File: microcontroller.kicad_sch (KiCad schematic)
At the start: 14 parts, among them SW201 SW_Push, U201 ESP32-S3-PICO-1-N8R2

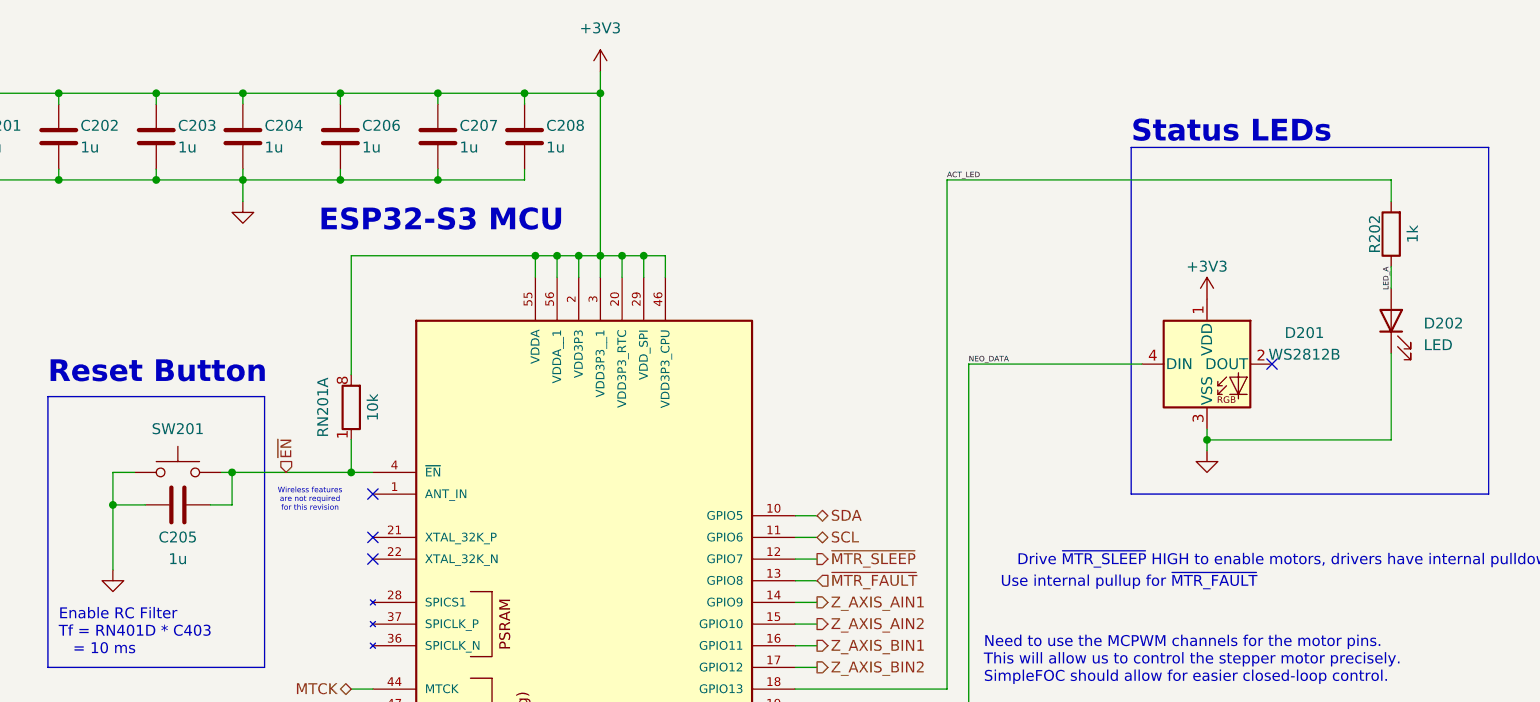
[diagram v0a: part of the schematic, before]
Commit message: Changed motor power supply
Removed 5V power rail. Migrated 3.3V rail to TPS62160
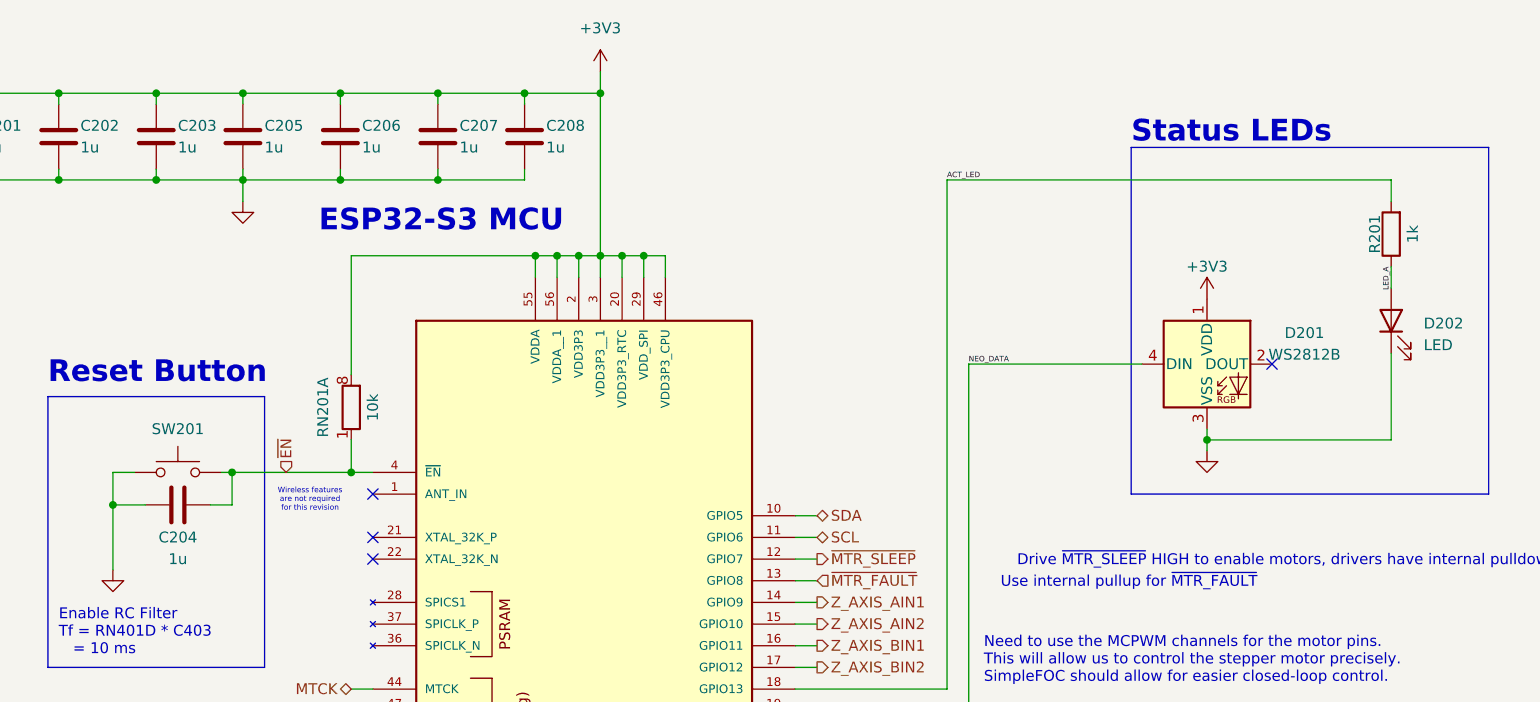
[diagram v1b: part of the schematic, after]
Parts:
- U201: footprint ESP32-S3-PICO-1-N8R2:PQFN40P700X700X106-57N -> SL_ST Tweezers:PQFN40P700X700X106-57N
- renumbered C205 to C204, C204 to C205, R202 to R201
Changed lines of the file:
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@@
 		(on_board yes)
 		(dnp no)
-		(property "Reference" "C204"
+		(property "Reference" "C205"
 			(at 102.87 27.94 0)
 			(effects
@@
 			(project "Vacuum_Tweezers"
 				(path "/25b5e35e-9397-4bb5-a91c-fc11ba49a08d/466683da-b970-4afc-a558-6e1093941948"
-					(reference "C204")
+					(reference "C205")
 					(unit 1)
 				)
@@
 		(on_board yes)
 		(dnp no)
-		(property "Reference" "#PWR0208"
+		(property "Reference" "#PWR0205"
 			(at 213.36 52.07 0)
 			(effects
@@
 			(project "Vacuum_Tweezers"
 				(path "/25b5e35e-9397-4bb5-a91c-fc11ba49a08d/466683da-b970-4afc-a558-6e1093941948"
-					(reference "#PWR0208")
+					(reference "#PWR0205")
 					(unit 1)
 				)
@@
 		(on_board yes)
 		(dnp no)
-		(property "Reference" "#PWR0201"
+		(property "Reference" "#PWR0203"
 			(at 142.24 25.4 0)
 			(effects
@@
 			(project "Vacuum_Tweezers"
 				(path "/25b5e35e-9397-4bb5-a91c-fc11ba49a08d/466683da-b970-4afc-a558-6e1093941948"
-					(reference "#PWR0201")
+					(reference "#PWR0203")
 					(unit 1)
 				)
@@
 			)
 		)
-		(property "Footprint" "ESP32-S3-PICO-1-N8R2:PQFN40P700X700X106-57N"
+		(property "Footprint" "SL_ST Tweezers:PQFN40P700X700X106-57N"
 			(at 144.78 93.98 0)
 			(effects
@@
 		(on_board yes)
 		(dnp no)
-		(property "Reference" "R202"
+		(property "Reference" "R201"
 			(at 233.045 40.64 90)
 			(effects
@@
 			(project "Vacuum_Tweezers"
 				(path "/25b5e35e-9397-4bb5-a91c-fc11ba49a08d/466683da-b970-4afc-a558-6e1093941948"
-					(reference "R202")
+					(reference "R201")
 					(unit 1)
 				)
@@
 		(dnp no)
 		(fields_autoplaced yes)
-		(property "Reference" "#PWR0209"
+		(property "Reference" "#PWR0206"
 			(at 213.36 72.39 0)
 			(effects
@@
 			(project "Vacuum_Tweezers"
 				(path "/25b5e35e-9397-4bb5-a91c-fc11ba49a08d/466683da-b970-4afc-a558-6e1093941948"
-					(reference "#PWR0209")
+					(reference "#PWR0206")
 					(unit 1)
 				)
@@
 		(dnp no)
 		(fields_autoplaced yes)
-		(property "Reference" "#PWR0203"
+		(property "Reference" "#PWR0201"
 			(at 85.09 86.36 0)
 			(effects
@@
 			(project "Vacuum_Tweezers"
 				(path "/25b5e35e-9397-4bb5-a91c-fc11ba49a08d/466683da-b970-4afc-a558-6e1093941948"
-					(reference "#PWR0203")
+					(reference "#PWR0201")
 					(unit 1)
 				)
@@
 		(on_board yes)
 		(dnp no)
-		(property "Reference" "C205"
+		(property "Reference" "C204"
 			(at 92.71 76.2 90)
 			(effects
@@
 			(project "Vacuum_Tweezers"
 				(path "/25b5e35e-9397-4bb5-a91c-fc11ba49a08d/466683da-b970-4afc-a558-6e1093941948"
-					(reference "C205")
+					(reference "C204")
 					(unit 1)
 				)
@@
 		(dnp no)
 		(fields_autoplaced yes)
-		(property "Reference" "#PWR0206"
+		(property "Reference" "#PWR0204"
 			(at 142.24 166.37 0)
 			(effects
@@
 			(project "Vacuum_Tweezers"
 				(path "/25b5e35e-9397-4bb5-a91c-fc11ba49a08d/466683da-b970-4afc-a558-6e1093941948"
-					(reference "#PWR0206")
-					(unit 1)
-				)
+					(reference "#PWR0204")
+					(unit 1)
+				)

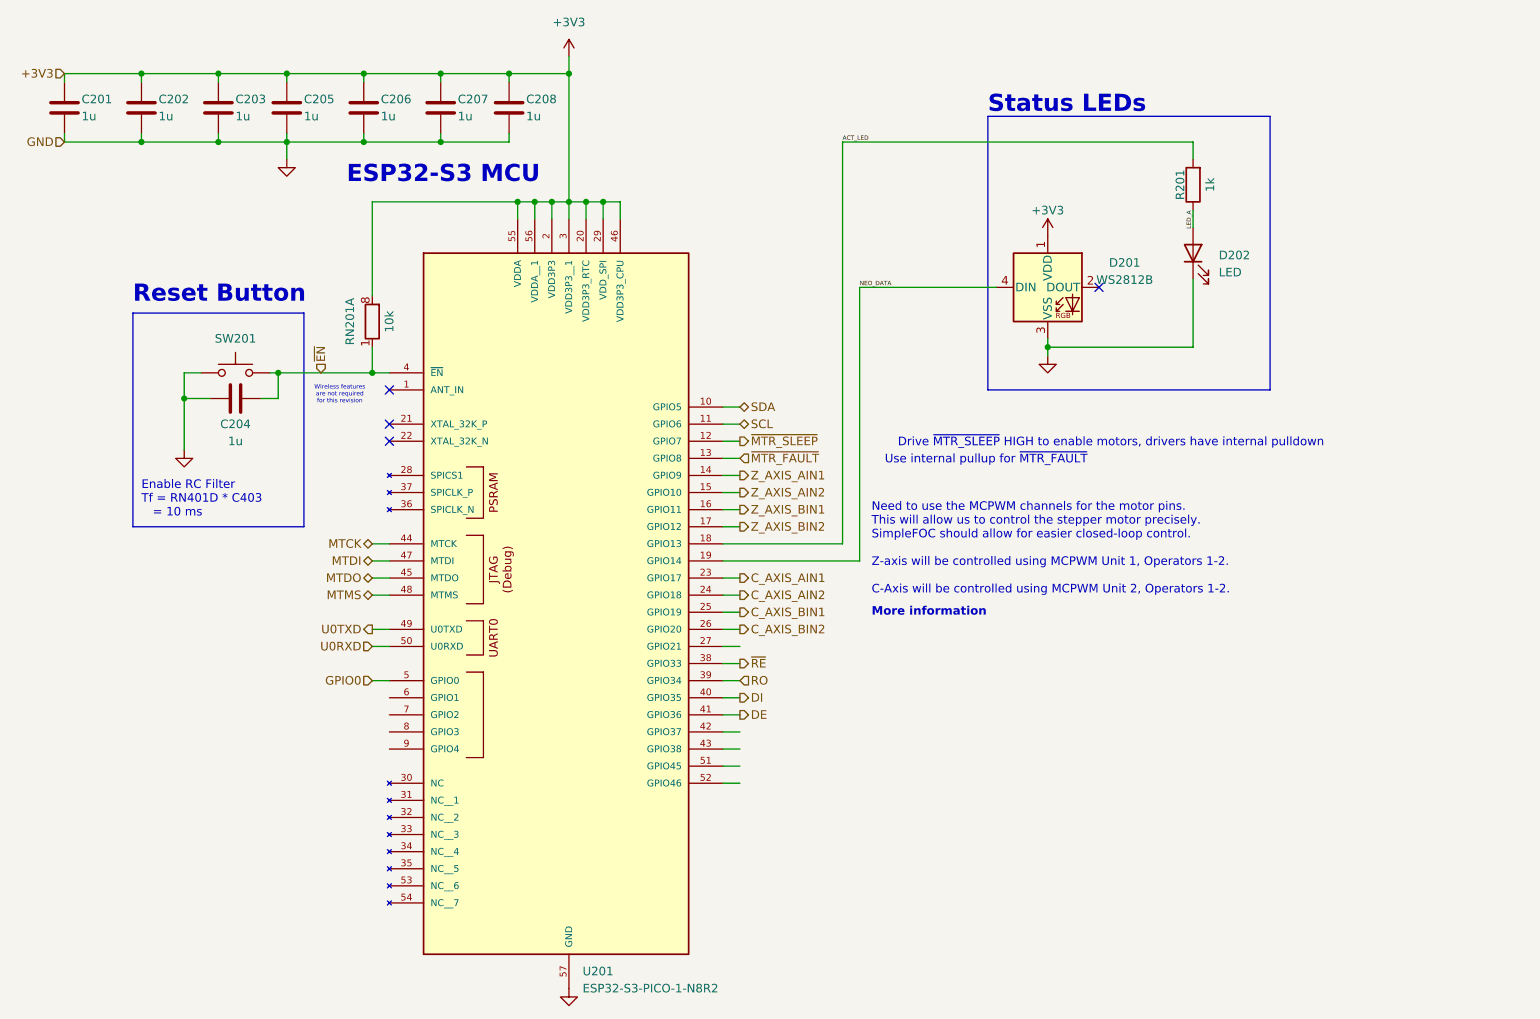
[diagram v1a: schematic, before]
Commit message: Finished Rev A1 PCB
Added all components and routed parts for Rev A1 PCB
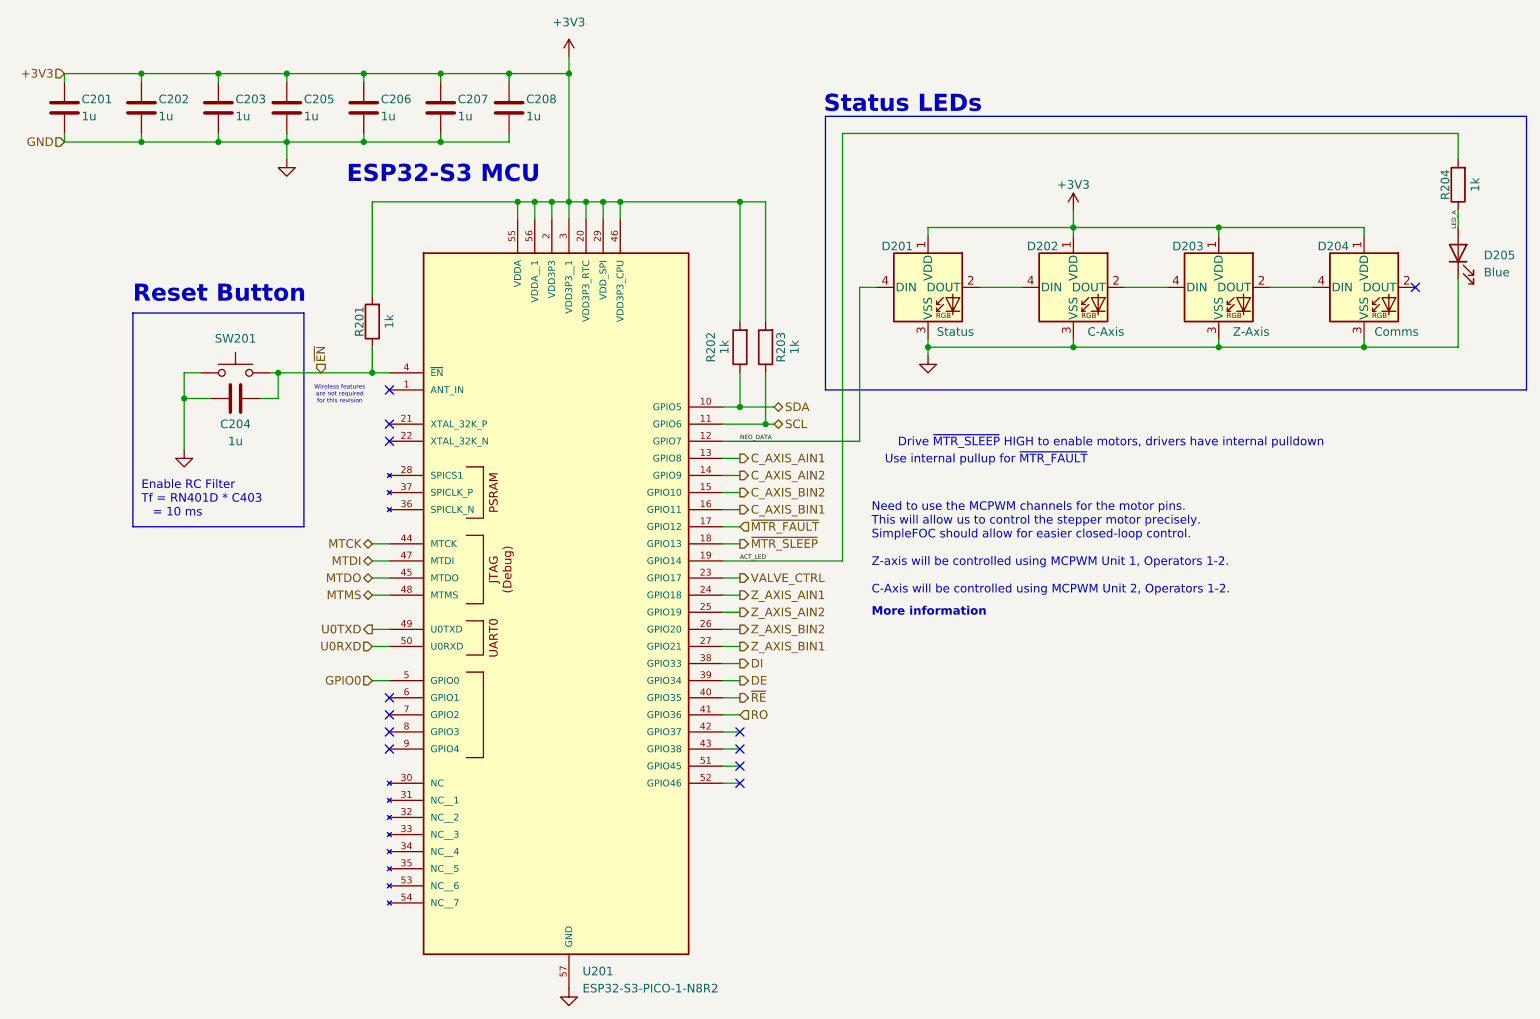
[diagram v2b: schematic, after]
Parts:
- removed RN201: 10k, Resistor_SMD:R_Array_Convex_4x0603, symbol Device:R_Pack04_Split
- added D202: C-Axis, LED_SMD:LED_WS2812B-2020_PLCC4_2.0x2.0mm, symbol LED:WS2812B
- added D203: Z-Axis, LED_SMD:LED_WS2812B-2020_PLCC4_2.0x2.0mm, symbol LED:WS2812B
- added D204: Comms, LED_SMD:LED_WS2812B-2020_PLCC4_2.0x2.0mm, symbol LED:WS2812B
- added R201, R202, R203: 1k, Resistor_SMD:R_0603_1608Metric, symbol Device:R
- D201: value WS2812B -> Status
- D205: renamed from D202; value LED -> Blue; footprint Diode_SMD:D_0603_1608Metric -> LED_SMD:LED_0603_1608Metric
- renumbered R201 to R204
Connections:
- net +3V3: now also D202.1 (VDD), D203.1 (VDD), D204.1 (VDD), R201.2, R202.2, R203.2
- net ACT_LED: now also U201.19 (GPIO14); no longer U201.18 (GPIO13)
- net C_AXIS_AIN1: now also U201.13 (GPIO8); no longer U201.23 (GPIO17)
- net C_AXIS_AIN2: now also U201.14 (GPIO9); no longer U201.24 (GPIO18)
- net C_AXIS_BIN1: now also U201.16 (GPIO11); no longer U201.25 (GPIO19)
- net C_AXIS_BIN2: now also U201.15 (GPIO10); no longer U201.26 (GPIO20)
- net DE: now also U201.39 (GPIO34); no longer U201.41 (GPIO36)
- net DI: now also U201.38 (GPIO33); no longer U201.40 (GPIO35)
- net GND: now also D202.3 (VSS), D203.3 (VSS), D204.3 (VSS)
- net NEO_DATA: now also U201.12 (GPIO7); no longer U201.19 (GPIO14)
- net RO: now also U201.41 (GPIO36); no longer U201.39 (GPIO34)
- net SCL: now also R203.1
- net SDA: now also R202.1
- net Z_AXIS_AIN1: now also U201.24 (GPIO18); no longer U201.14 (GPIO9)
- net Z_AXIS_AIN2: now also U201.25 (GPIO19); no longer U201.15 (GPIO10)
- net Z_AXIS_BIN1: now also U201.27 (GPIO21); no longer U201.16 (GPIO11)
- net Z_AXIS_BIN2: now also U201.26 (GPIO20); no longer U201.17 (GPIO12)
- net ~{EN}: now also R201.1
- net ~{MTR_FAULT}: now also U201.17 (GPIO12); no longer U201.13 (GPIO8)
- net ~{MTR_SLEEP}: now also U201.18 (GPIO13); no longer U201.12 (GPIO7)
- net ~{RE}: now also U201.40 (GPIO35); no longer U201.38 (GPIO33)
- net at D201.2 (DOUT): now also D202.4 (DIN)
- new net: D202.2 (DOUT), D203.4 (DIN)
- new net: D203.2 (DOUT), D204.4 (DIN)
- new net VALVE_CTRL: U201.23 (GPIO17)
- no-connect marks 4 -> 12
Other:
- moved on the sheet: D201, D205, R204

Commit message: Fixed footprint reference
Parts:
- D205: footprint LED_SMD:LED_0603_1608Metric -> LED_SMD:LED_0603_1608Metric
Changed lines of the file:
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@@
 			)
 		)
-		(property "Footprint" "LED_SMD:LED_0603_1608Metric "
+		(property "Footprint" "LED_SMD:LED_0603_1608Metric"
 			(at 274.32 50.8 0)
 			(effects
